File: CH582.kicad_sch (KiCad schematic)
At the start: 47 parts, among them J1 Conn_01x02, J2 Conn_01x02, J3 Peripherals, SW2 POWER, U2 XC6220B331QR-G, U3 M3406, Y1 32MHz, Y2 Crystal_Small

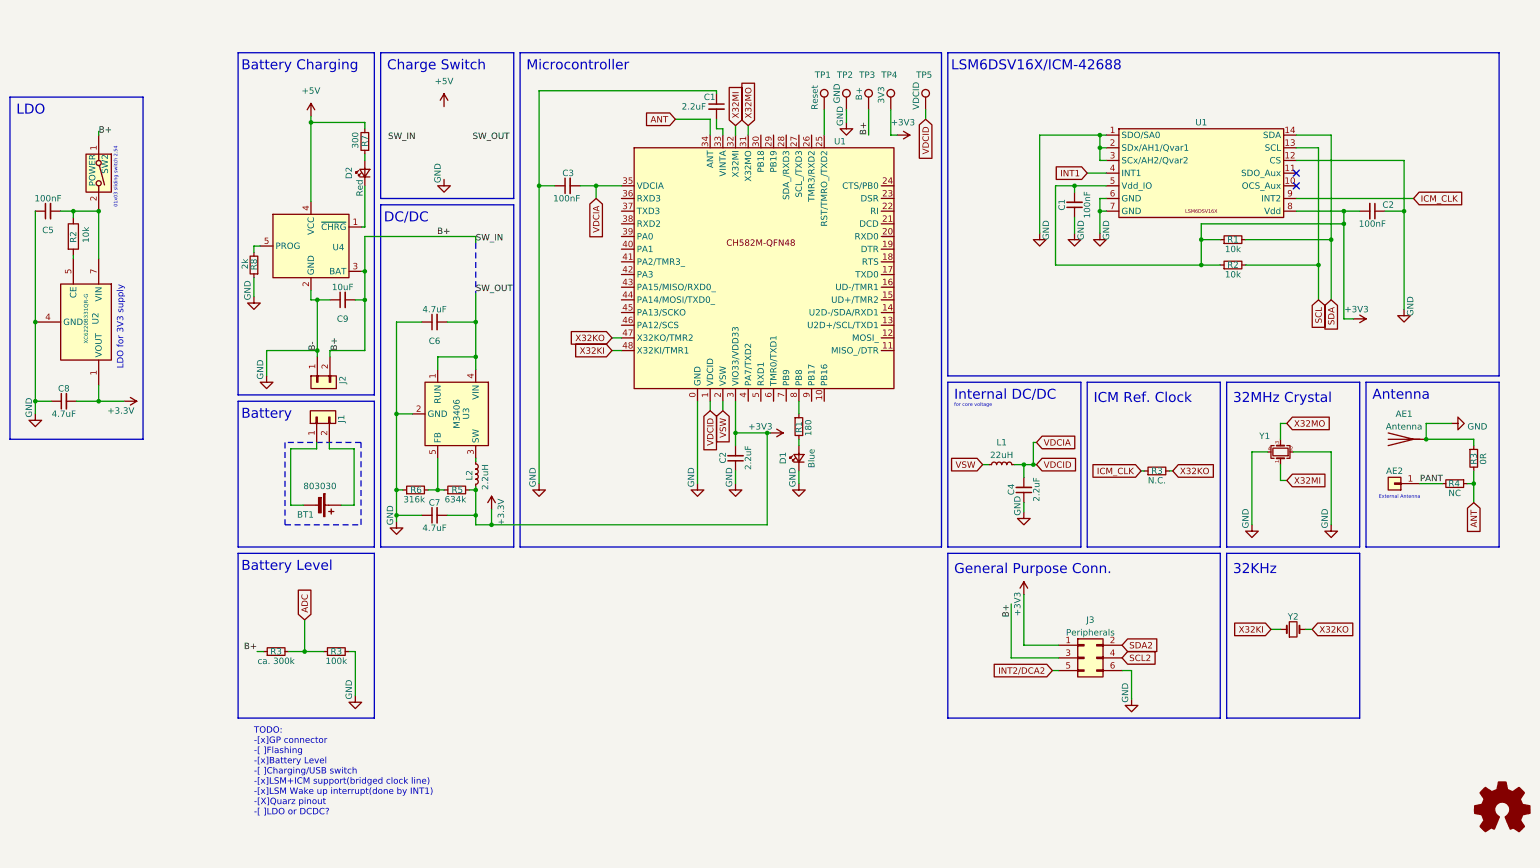
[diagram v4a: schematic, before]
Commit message: added USB flashing interface, rgb led, mounting hole
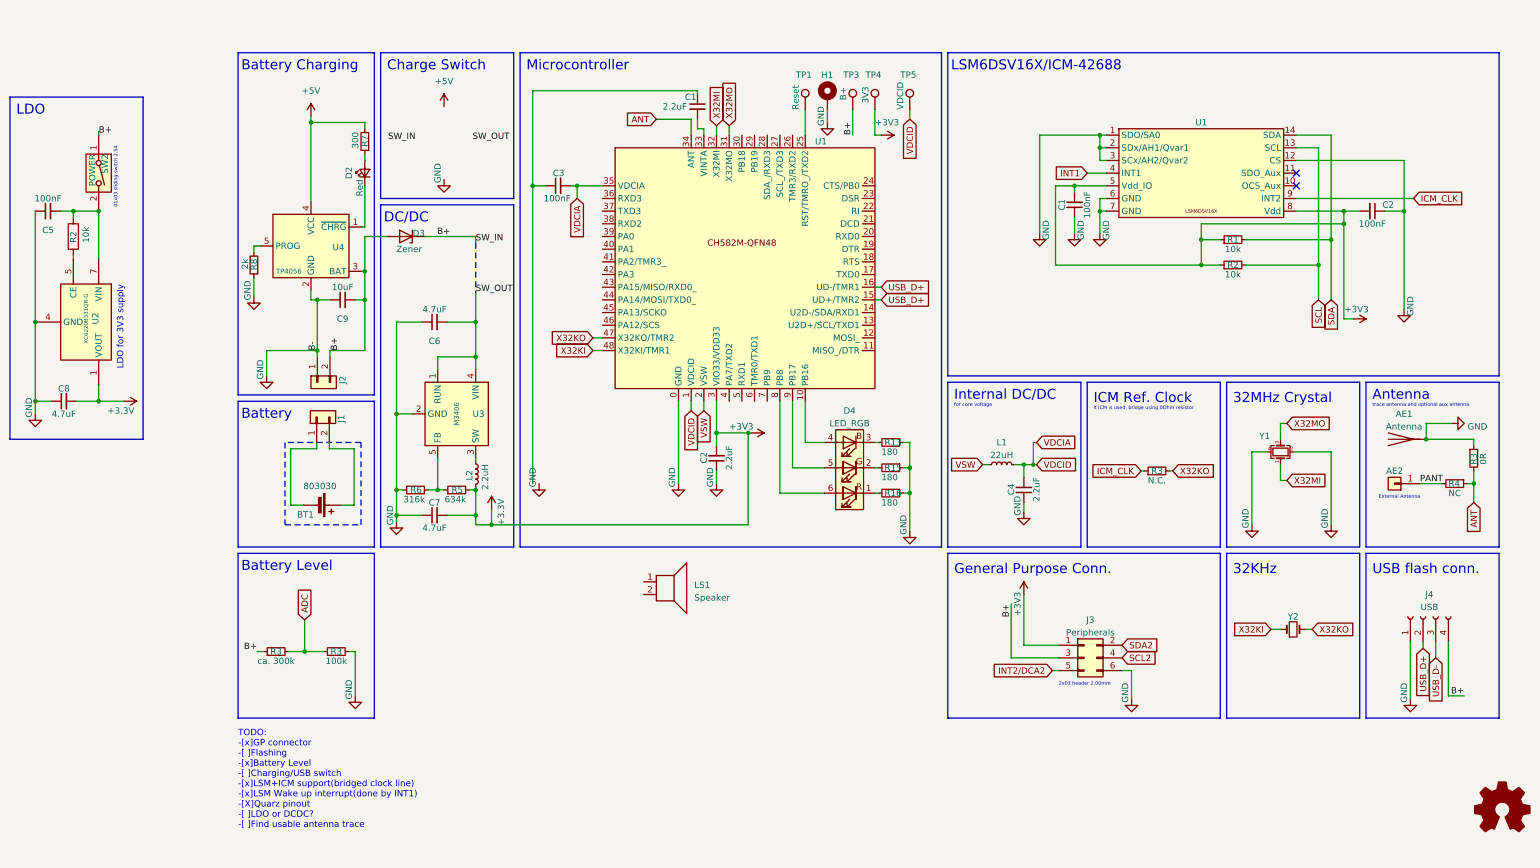
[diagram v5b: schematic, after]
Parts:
- removed D1: Blue, symbol Device:LED_Small
- removed R1: 180, symbol Device:R_Small
- removed TP2: GND, symbol Connector:TestPoint
- added D3: Zener, symbol Device:D_Zener
- added D4: LED_RGB, symbol Device:LED_RGB
- added H1: MountingHole_Pad, symbol Mechanical:MountingHole_Pad
- added J4: USB, symbol Connector:Conn_01x04_Socket
- added LS1: Speaker, symbol Device:Speaker
- added R13, R15, R16: 180, symbol Device:R_Small
- U4: value ~ -> TP4056
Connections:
- net B+: now also D3.1 (K), D3.2 (A), J4.4 (Pin_4)
- net GND: now also H1.1, J4.1 (Pin_1), R13.1, R15.1, R16.1; no longer C1.1, C3.1
- net at U1.8 (PB8): now also D4.6 (RA)
- net at U1.10 (PB16): now also D4.4 (BA)
- net USB_D+: now reaches U1.15 (UD+/TMR2)
- net USB_D+: now also U1.16 (UD-/TMR1), J4.2 (Pin_2)
- net at U1.9 (PB17): now also D4.5 (GA)
- new net: C1.1, C3.1
- new net: D4.1 (RK), R16.2
- new net: D4.2 (GK), R15.2
- new net: D4.3 (BK), R13.2
- new net USB_D-: J4.3 (Pin_3)
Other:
- note added: "2x03 header 2.00mm"
- note added: "TODO: -[x]GP connector -[ ]Flashing -[x]Battery Level -[ ]Charging/USB switch -[x]LSM+ICM support(bridged clock line) -[x]LSM Wake up interrupt(done by INT1) -[X]Quarz pinout -[ ]LDO or DCDC? -[ ]Find usable antenna trace"
- note added: "USB flash conn."
- note added: "if ICM is used, bridge using 0Ohm resistor"
- note added: "trace antenna and optional aux antenna"
- note removed: "TODO: -[x]GP connector -[ ]Flashing -[x]Battery Level -[ ]Charging/USB switch -[x]LSM+ICM support(bridged clock line) -[x]LSM Wake up interrupt(done by INT1) -[X]Quarz pinout -[ ]LDO or DCDC?"
- moved on the sheet: C1, C2, C3, TP1, TP3, TP4, TP5, U1
